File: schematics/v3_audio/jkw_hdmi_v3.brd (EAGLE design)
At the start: 40.9 x 50 mm, 50 parts, among them J1 2X20-CHIP-HEADERS, J3 T_MOLEX_45171, Q2 12mhz, U1 DS2431P, U2 LP5907MFX

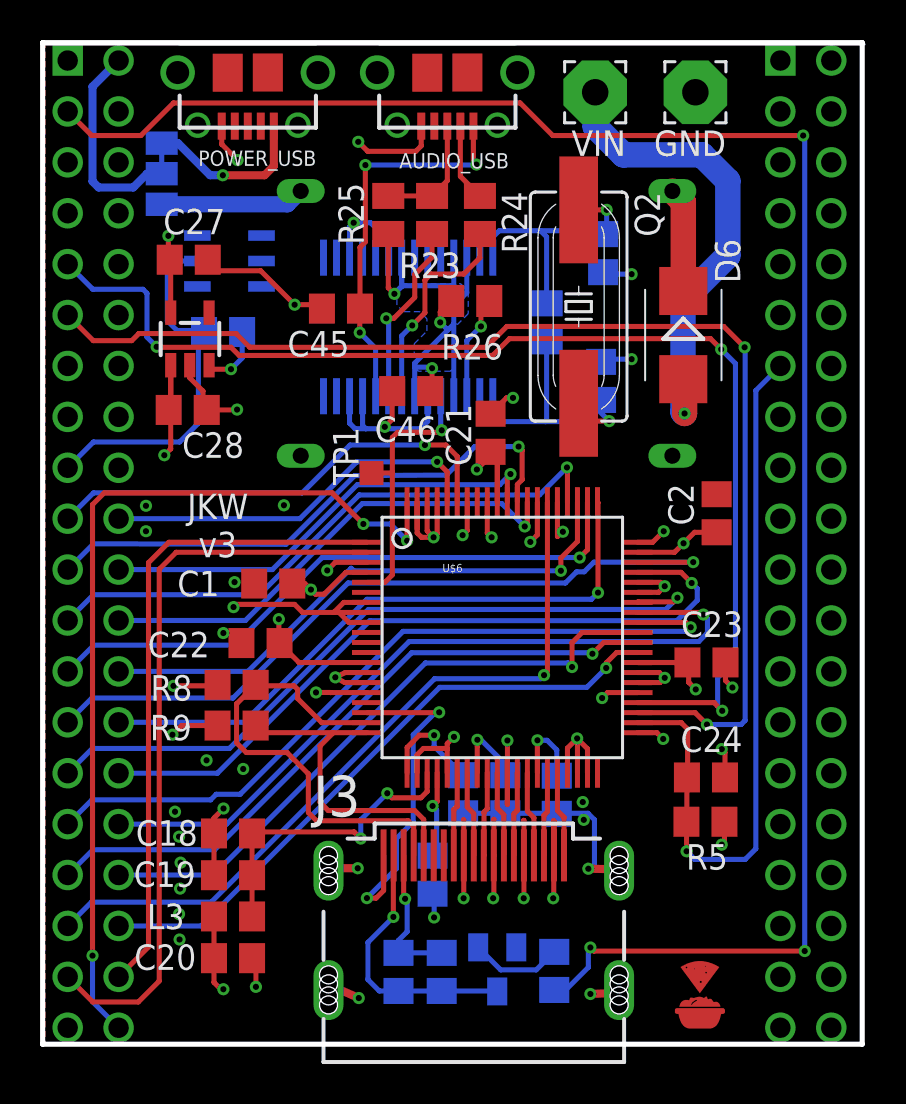
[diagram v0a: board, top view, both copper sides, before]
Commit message: updated routing for LCD length matching
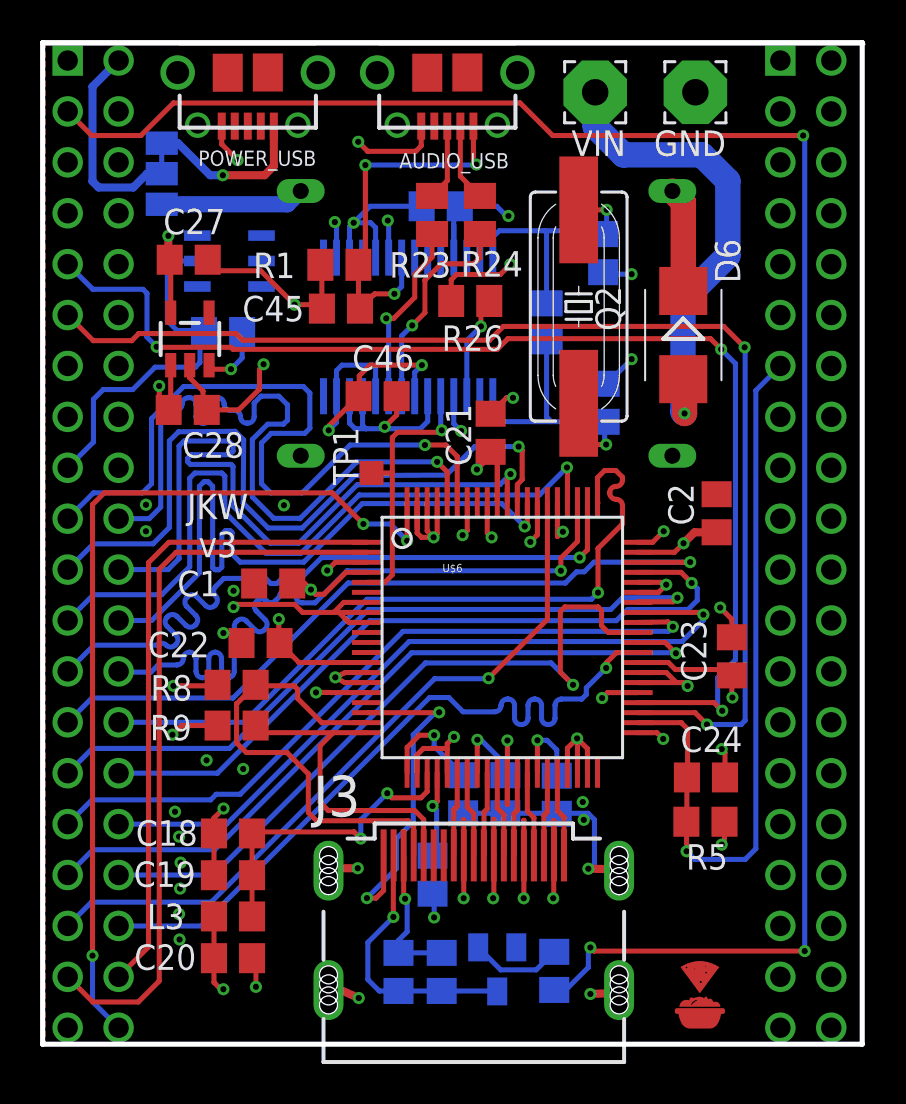
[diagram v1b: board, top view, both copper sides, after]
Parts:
- removed R25: 1k5, rcl:M0805
- added C3: n.a., rcl:C0805
- added R1: 1M, rcl:M0805
- moved C46 1.70 mm to (16.7, 32.3), turned to 0 degrees
- moved C23 1.31 mm to (34.4, 19.4), turned to 90 degrees
- moved C44 1.11 mm to (28.0, 32.0)
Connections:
- net N$11 renamed TXC-
- net N$14 renamed TXC+
- net N$15 renamed TX2+
- net N$16 renamed TX2-
- net N$17 renamed TX1+
- net N$18 renamed TX1-
- net N$19 renamed TX0+
- net N$20 renamed TX0-
- net N$57 renamed XTO
- net N$58 renamed XTI
- removed net N$66: AUDIO_USB.VBUS, C45.2, U$5.10
- removed net VCCL: U$5.13
- removed net VCCP: U$5.20
- removed net VCCR: U$5.16
- net GND: now also C3.2, R1.2, U$5.4
- net N$62: no longer R25.1
- net VCC: now also C3.1, C46.1, R26.1, U$5.10, U$5.13, U$5.16, U$5.20, U$5.25, U$5.26, U$5.7
- net VCC2: now also AUDIO_USB.VBUS, C45.2, R1.1; no longer C46.1, R25.2, R26.1, U$5.25, U$5.26, U$5.4, U$5.7
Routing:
- net VCC: track 48.3 -> 79.3 mm, vias 12 -> 18
- net N$66: track 19.5 -> 0.00 mm, vias 3 -> 0
- net LCD-D3: track 19.3 -> 35.7 mm
- net GND: track 139.4 -> 153.0 mm, vias 51 -> 52
- net LCD-D5: track 23.0 -> 36.5 mm
- net LCD-D4: track 23.5 -> 36.8 mm
- net LCD-D7: track 24.4 -> 35.9 mm
- net 1.8V: track 96.5 -> 87.7 mm
- net LCD-D6: track 28.1 -> 36.5 mm
- net VCC2: track 26.9 -> 18.9 mm
- net LCD-D10: track 29.8 -> 36.8 mm
- net LCD-D11: track 28.0 -> 34.9 mm
- net LCD-D13: track 31.1 -> 36.2 mm
- net LCD-D12: track 30.8 -> 35.4 mm
- net LCD-D21: track 31.8 -> 36.4 mm
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- removed copper zone on layer 16, net VCC2
